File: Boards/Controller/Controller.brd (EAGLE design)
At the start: 74.9 x 74.6 mm, 16 parts, among them J1 POWER_JACKPTH_BREAD

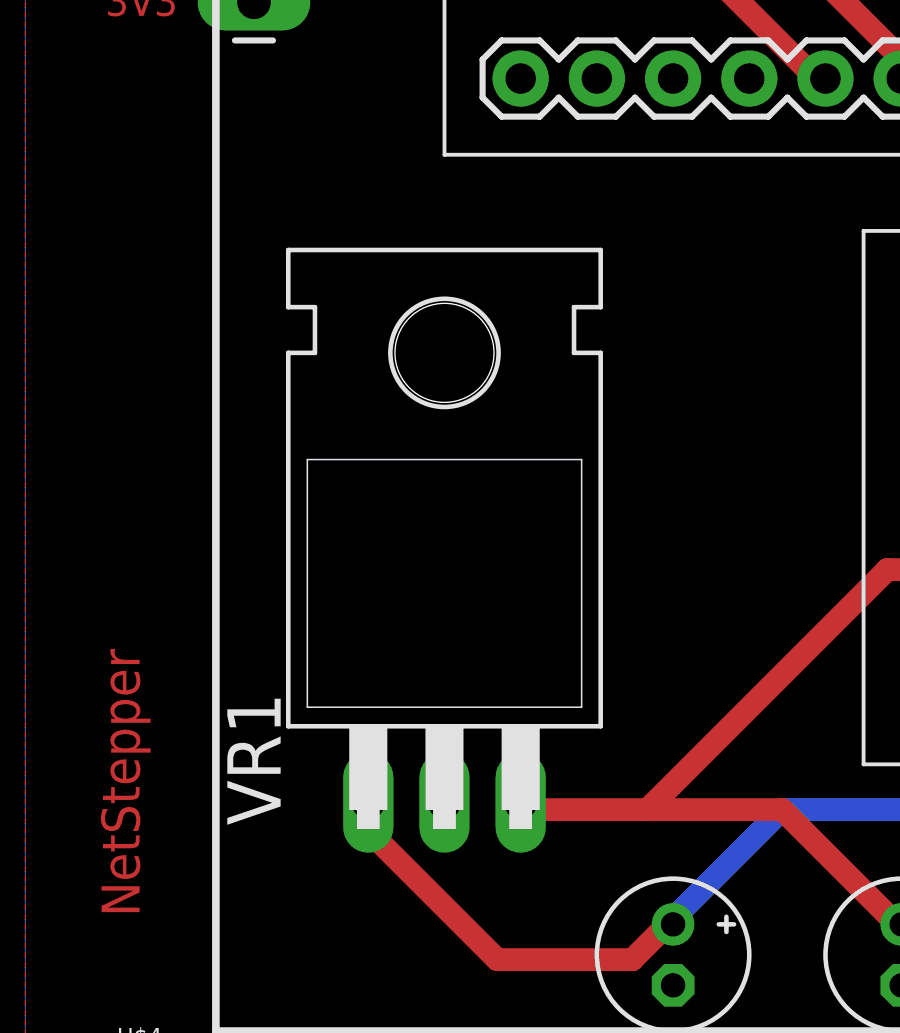
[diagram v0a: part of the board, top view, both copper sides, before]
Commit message: use stepping voltage regulator instead of a linear
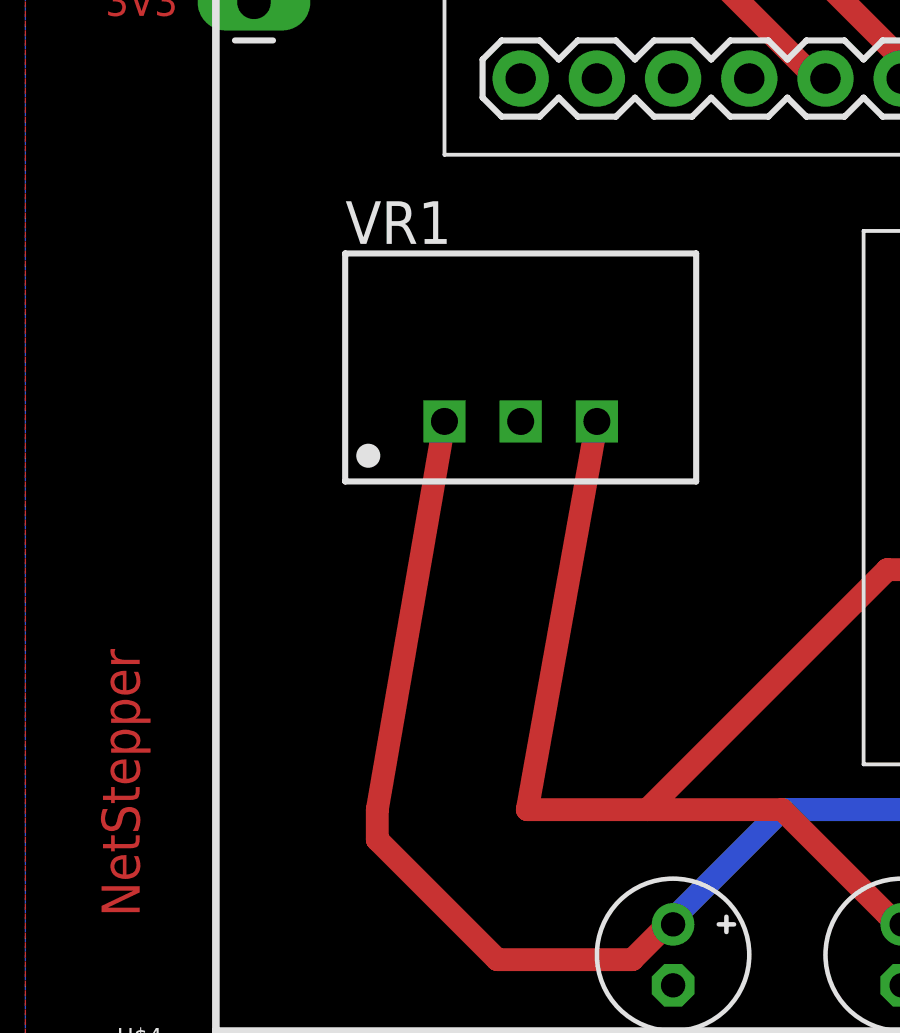
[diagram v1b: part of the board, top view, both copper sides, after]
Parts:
- VR1: value 7805T -> TSR_1-2450; device adafruit:TO220H -> Traco-TSR1:TSR-1
- moved VR1 3.59 mm to (17.8, 27.9)
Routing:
- net 5V: track 66.2 -> 79.0 mm
- net 12V: track 68.5 -> 81.2 mm
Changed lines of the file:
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@@
 <attribute name="PROD_ID" value="CONN-09696" x="36.83" y="8.89" size="1.778" layer="27" display="off"/>
 </element>
-<element name="VR1" library="adafruit" package="TO220H" value="7805T" x="15.24" y="25.4"/>
+<element name="VR1" library="Traco-TSR1" package="TSR-1" value="TSR_1-2450" x="17.78" y="27.94"/>
 <element name="C1" library="adafruit" package="E2-5" value="10uF" x="22.86" y="10.16" rot="R270"/>
 <element name="C2" library="adafruit" package="E2-5" value="10uF" x="30.48" y="10.16" rot="R270"/>
@@
 <wire x1="13" y1="15" x2="13" y2="14" width="0.762" layer="1"/>
 <wire x1="22.5" y1="11" x2="22.86" y2="11.176" width="0.762" layer="1"/>
-<wire x1="13" y1="15" x2="12.7" y2="15.24" width="0.762" layer="1"/>
+<wire x1="13" y1="15" x2="15.24" y2="27.94" width="0.762" layer="1"/>
 <wire x1="54.5" y1="9" x2="51" y2="9" width="0.762" layer="16"/>
 <wire x1="59.5" y1="14" x2="56.25" y2="10.75" width="0.762" layer="16"/>
@@
 <wire x1="22" y1="15" x2="26.5" y2="15" width="0.762" layer="1"/>
 <wire x1="30" y1="11.5" x2="30.48" y2="11.176" width="0.762" layer="1"/>
-<wire x1="18" y1="15" x2="17.78" y2="15.24" width="0.762" layer="1"/>
+<wire x1="18" y1="15" x2="20.32" y2="27.94" width="0.762" layer="1"/>
 <wire x1="47.5" y1="23" x2="63.5" y2="39" width="0.762" layer="1"/>
 <wire x1="30" y1="23" x2="47.5" y2="23" width="0.762" layer="1"/>
